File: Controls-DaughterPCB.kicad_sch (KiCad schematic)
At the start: 17 parts, among them U8 LMC555xM

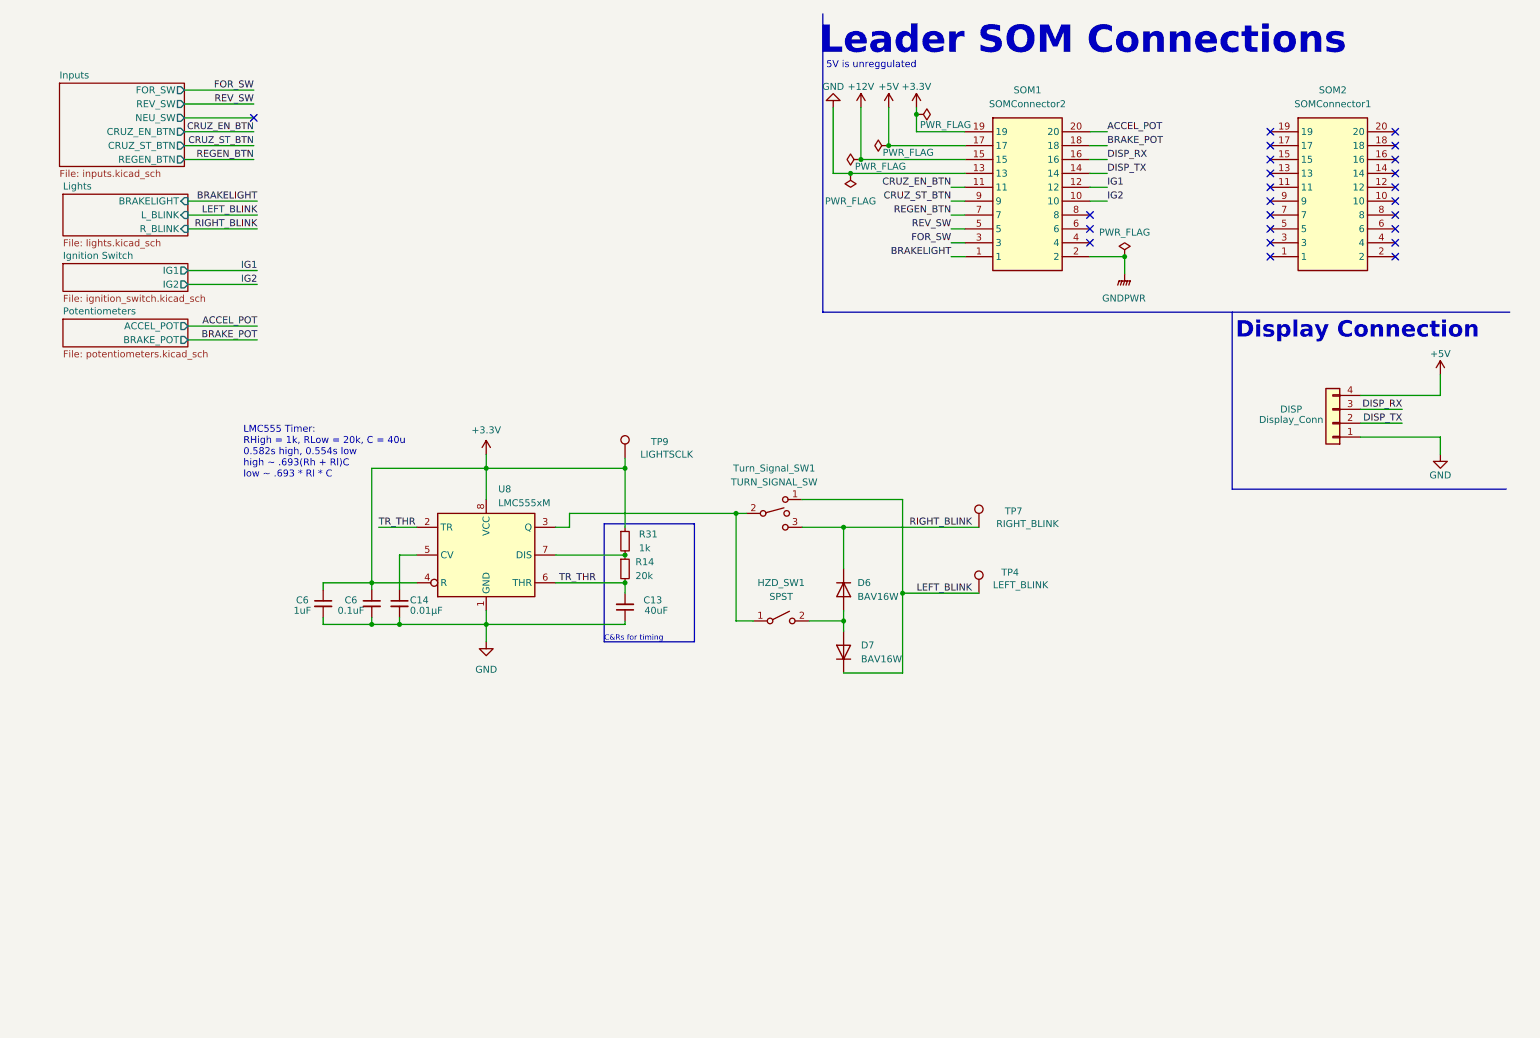
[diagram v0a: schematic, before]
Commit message: changed resistor values, updated footprints
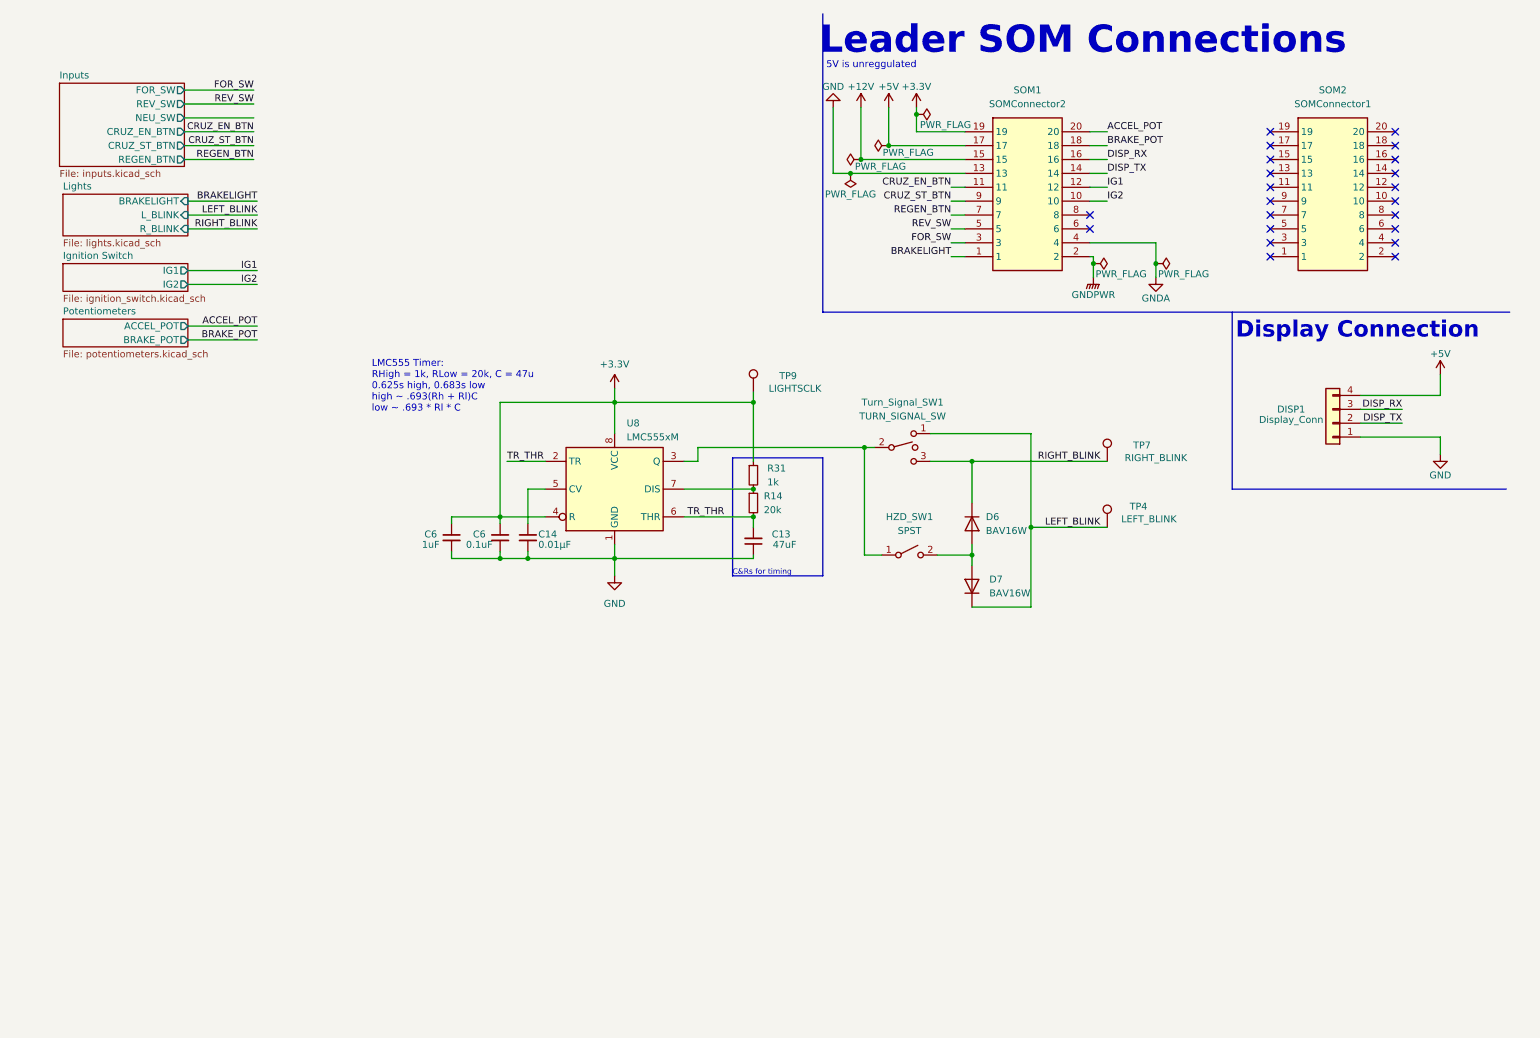
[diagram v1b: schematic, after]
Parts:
- C13: value 40uF -> 47uF; footprint (none) -> Capacitor_SMD:C_0805_2012Metric; Mouser Part Number (none) -> 81-GRM21BR61A476ME5L; P/N (none) -> GRM21BR61A476ME15L
- C14: footprint (none) -> Capacitor_SMD:C_0805_2012Metric; Mouser Part Number (none) -> 80-C0805C103J5R; P/N (none) -> C0805C103J5RACTU
- C6: footprint (none) -> Capacitor_SMD:C_0805_2012Metric; Mouser Part Number (none) -> 80-C0805C105K5P; P/N (none) -> C0805C105K5PACTU
- C6: footprint (none) -> Capacitor_SMD:C_0805_2012Metric; Mouser Part Number (none) -> 80-C0805C104M5R; P/N (none) -> C0805C104M5RACTU
- DISP1: renamed from DISP; footprint (none) -> Connector_Molex:Molex_Micro-Fit_3.0_43650-0415_1x04_P3.00mm_Vertical; Mouser Part Number (none) -> 538-43650-0415; P/N (none) -> 43650-0415
- R14: footprint (none) -> Resistor_SMD:R_0805_2012Metric; Mouser Part Number (none) -> 603-RP0805BRD0720KL; P/N (none) -> RP0805BRD0720KL
- R31: footprint (none) -> Resistor_SMD:R_0805_2012Metric; Mouser Part Number (none) -> 71-CRCW08051K00FKEAC; P/N (none) -> CRCW08051K00FKEAC
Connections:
- net GNDA: now reaches SOM1.4
- no-connect marks 24 -> 22
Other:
- note added: "LMC555 Timer: RHigh = 1k, RLow = 20k, C = 47u 0.625s high, 0.683s low high ~ .693(Rh + Rl)C low ~ .693 * Rl * C"
- note removed: "LMC555 Timer: RHigh = 1k, RLow = 20k, C = 40u 0.582s high, 0.554s low high ~ .693(Rh + Rl)C low ~ .693 * Rl * C"
- moved on the sheet: C13, C14, C6, D6, D7, HZD_SW1, R14, R31, TP4, TP7, TP9, Turn_Signal_SW1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

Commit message: added mounting holes & silkscreen images, created fans sheet
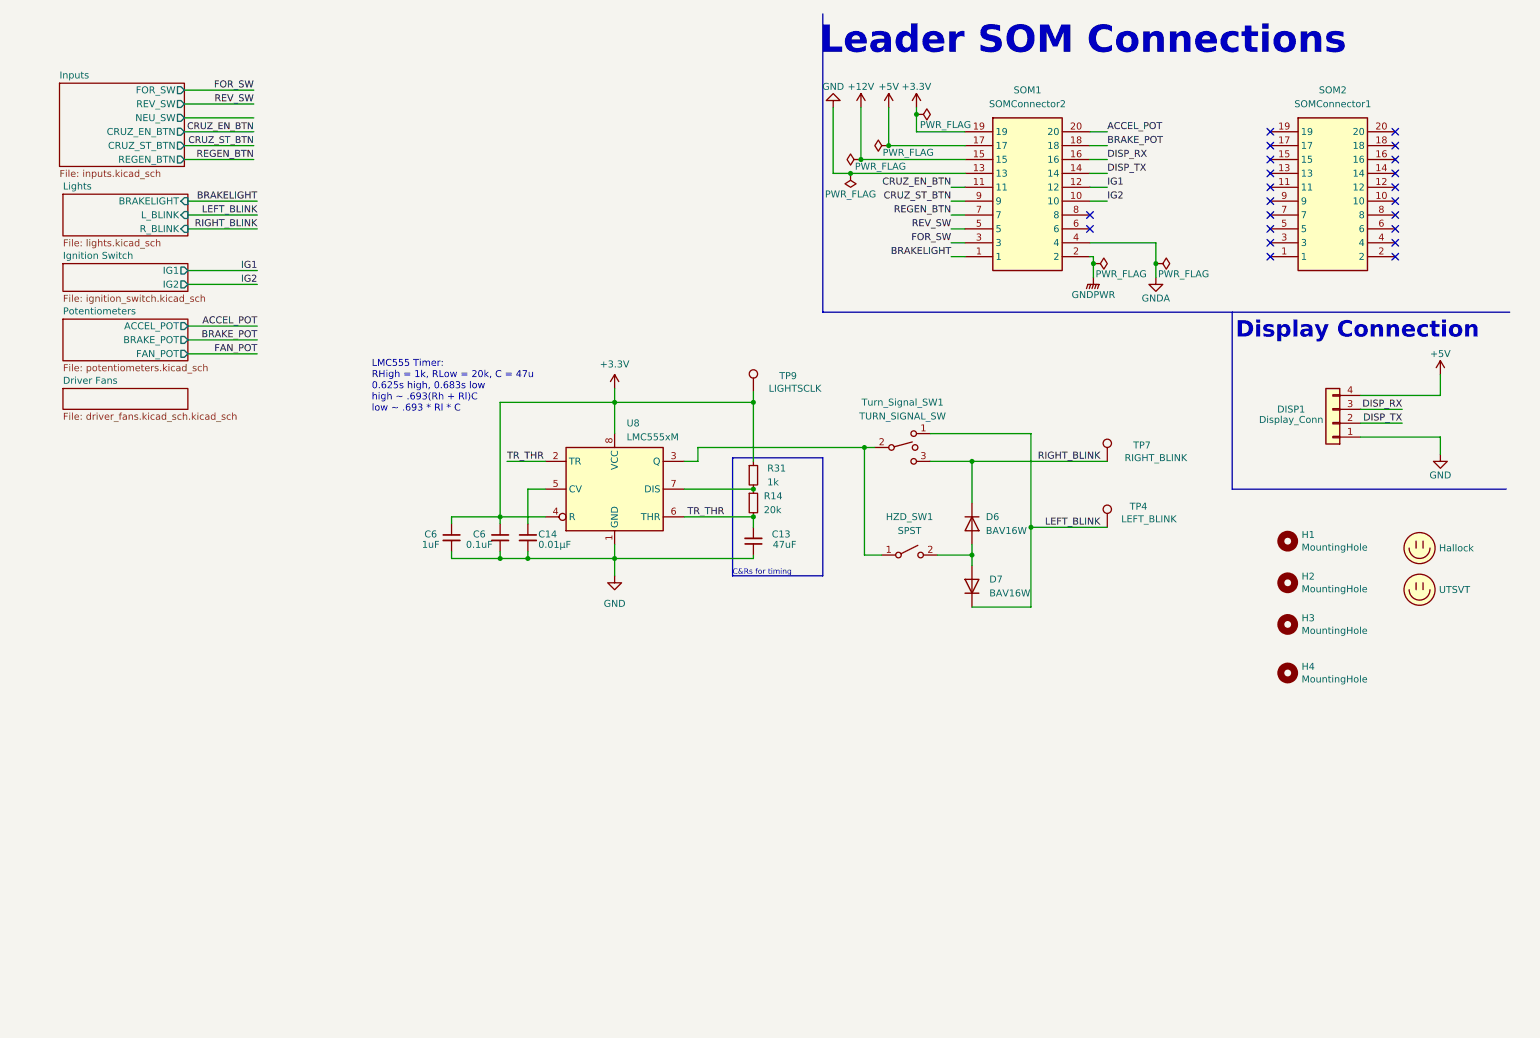
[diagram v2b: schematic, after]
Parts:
- added H1, H2, H3, H4: MountingHole, MountingHole:MountingHole_3mm, symbol Mechanical:MountingHole
- added LOGO1: Hallock, UTSVT_Special:Hallock_Image_Small, symbol utsvt-misc:Logo_Placeholder
- added LOGO2: UTSVT, UTSVT_Special:UTSVT_Logo_Symbol, symbol utsvt-misc:Logo_Placeholder
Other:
- added sheet Driver Fans (driver_fans.kicad_sch.kicad_sch)
- sheet Potentiometers ports: added FAN_POT; removed none
- note removed: "5V is unreggulated"
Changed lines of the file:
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@@
+    (stroke (width 0) (type default))
+  )
+  (wire (pts (xy 44.45 73.66) (xy 57.15 73.66))
     (stroke (width 0) (type default))
   )
@@
     (effects (font (size 1.27 1.27)) (justify left bottom))
   )
-  (text "5V is unreggulated\n" (at 161.29 21.59 0)
-    (effects (font (size 1.27 1.27)) (justify left bottom))
-  )
   (label "REGEN_BTN" (at 56.515 38.1 180) (fields_autoplaced)
     (effects (font (size 1.27 1.27)) (justify right bottom))
@@
   (label "DISP_RX" (at 212.725 38.1 0) (fields_autoplaced)
     (effects (font (size 1.27 1.27)) (justify left bottom))
+  )
+  (label "FAN_POT" (at 57.15 73.66 180) (fields_autoplaced)
+    (effects (font (size 1.27 1.27)) (justify right bottom))
   )
   (label "ACCEL_POT" (at 212.725 33.02 0) (fields_autoplaced)
@@
     )
   )
+  (symbol (lib_id "Mechanical:MountingHole") (at 245.745 115.57 0) (unit 1)
+    (in_bom yes) (on_board yes) (dnp no)
+    (property "Reference" "H2" (at 248.285 114.4016 0)
+      (effects (font (size 1.27 1.27)) (justify left))
+    )
+    (property "Value" "MountingHole" (at 248.285 116.713 0)
+      (effects (font (size 1.27 1.27)) (justify left))
+    )
+    (property "Footprint" "MountingHole:MountingHole_3mm" (at 245.745 115.57 0)
+      (effects (font (size 1.27 1.27)) hide)
+    )
+    (property "Datasheet" "~" (at 245.745 115.57 0)
+      (effects (font (size 1.27 1.27)) hide)
+    )
+    (instances
+      (project "Controls-DaughterPCB"
+        (path "/c7871779-04fe-4705-8150-20a4dd0ef44f"
+          (reference "H2") (unit 1)
+        )
+      )
+      (project "BPS-Fan"
+        (path "/e60847d4-a954-40b9-b9c4-54b73957661c"
+          (reference "H2") (unit 1)
+        )
+      )
+    )
+  )
   (symbol (lib_id "Connector:TestPoint") (at 212.725 105.41 0) (unit 1)
     (in_bom yes) (on_board yes) (dnp no)
@@
         (path "/c7871779-04fe-4705-8150-20a4dd0ef44f"
           (reference "#FLG01") (unit 1)
+        )
+      )
+    )
+  )
+  (symbol (lib_id "utsvt-misc:Logo_Placeholder") (at 269.875 109.22 0) (unit 1)
+    (in_bom yes) (on_board yes) (dnp no)
+    (property "Reference" "LOGO1" (at 269.875 105.41 0)
+      (effects (font (size 1.27 1.27)) hide)
+    )
+    (property "Value" "Hallock" (at 273.431 109.22 0)
+      (effects (font (size 1.27 1.27)) (justify left))
+    )
+    (property "Footprint" "UTSVT_Special:Hallock_Image_Small" (at 269.875 107.315 0)
+      (effects (font (size 1.27 1.27)) hide)
+    )
+    (property "Datasheet" "" (at 269.875 107.315 0)
+      (effects (font (size 1.27 1.27)) hide)
+    )
+    (instances
+      (project "Controls-DaughterPCB"
+        (path "/c7871779-04fe-4705-8150-20a4dd0ef44f"
+          (reference "LOGO1") (unit 1)
+        )
+      )
+      (project "BPS-Fan"
+        (path "/e60847d4-a954-40b9-b9c4-54b73957661c"
+          (reference "LOGO1") (unit 1)
         )
       )
@@
     )
   )
+  (symbol (lib_id "Mechanical:MountingHole") (at 245.745 132.08 0) (unit 1)
+    (in_bom yes) (on_board yes) (dnp no)
+    (property "Reference" "H4" (at 248.285 130.9116 0)
+      (effects (font (size 1.27 1.27)) (justify left))
+    )
+    (property "Value" "MountingHole" (at 248.285 133.223 0)
+      (effects (font (size 1.27 1.27)) (justify left))
+    )
+    (property "Footprint" "MountingHole:MountingHole_3mm" (at 245.745 132.08 0)
+      (effects (font (size 1.27 1.27)) hide)
+    )
+    (property "Datasheet" "~" (at 245.745 132.08 0)
+      (effects (font (size 1.27 1.27)) hide)
+    )
+    (instances
+      (project "Controls-DaughterPCB"
+        (path "/c7871779-04fe-4705-8150-20a4dd0ef44f"
+          (reference "H4") (unit 1)
+        )
+      )
+      (project "BPS-Fan"
+        (path "/e60847d4-a954-40b9-b9c4-54b73957661c"
+          (reference "H4") (unit 1)
+        )
+      )
+    )
+  )
   (symbol (lib_id "Device:C_Small") (at 106.68 107.315 0) (unit 1)
     (in_bom yes) (on_board yes) (dnp no)
@@
     )
   )
+  (symbol (lib_id "utsvt-misc:Logo_Placeholder") (at 269.875 116.84 0) (unit 1)
+    (in_bom yes) (on_board yes) (dnp no)
+    (property "Reference" "LOGO2" (at 269.875 113.03 0)
+      (effects (font (size 1.27 1.27)) hide)
+    )
+    (property "Value" "UTSVT" (at 273.431 116.84 0)
+      (effects (font (size 1.27 1.27)) (justify left))
+    )
+    (property "Footprint" "UTSVT_Special:UTSVT_Logo_Symbol" (at 269.875 114.935 0)
+      (effects (font (size 1.27 1.27)) hide)
+    )
+    (property "Datasheet" "" (at 269.875 114.935 0)
+      (effects (font (size 1.27 1.27)) hide)
+    )
+    (instances
+      (project "Controls-DaughterPCB"
+        (path "/c7871779-04fe-4705-8150-20a4dd0ef44f"
+          (reference "LOGO2") (unit 1)
+        )
+      )
+      (project "BPS-Fan"
+        (path "/e60847d4-a954-40b9-b9c4-54b73957661c"
+          (reference "LOGO2") (unit 1)
+        )
+      )
+    )
+  )
   (symbol (lib_id "power:PWR_FLAG") (at 177.8 29.845 270) (unit 1)
     (in_bom yes) (on_board yes) (dnp no)
@@
         (path "/c7871779-04fe-4705-8150-20a4dd0ef44f"
           (reference "#FLG02") (unit 1)
+        )
+      )
+    )
+  )
+  (symbol (lib_id "Mechanical:MountingHole") (at 245.745 107.95 0) (unit 1)
+    (in_bom yes) (on_board yes) (dnp no)
+    (property "Reference" "H1" (at 248.285 106.7816 0)
+      (effects (font (size 1.27 1.27)) (justify left))
+    )
+    (property "Value" "MountingHole" (at 248.285 109.093 0)
+      (effects (font (size 1.27 1.27)) (justify left))
+    )
+    (property "Footprint" "MountingHole:MountingHole_3mm" (at 245.745 107.95 0)
+      (effects (font (size 1.27 1.27)) hide)
+    )
+    (property "Datasheet" "~" (at 245.745 107.95 0)
+      (effects (font (size 1.27 1.27)) hide)
+    )
+    (instances
+      (project "Controls-DaughterPCB"
+        (path "/c7871779-04fe-4705-8150-20a4dd0ef44f"
+          (reference "H1") (unit 1)
+        )
+      )
+      (project "BPS-Fan"
+        (path "/e60847d4-a954-40b9-b9c4-54b73957661c"
+          (reference "H1") (unit 1)
         )
       )
@@
     )
   )
+  (symbol (lib_id "Mechanical:MountingHole") (at 245.745 123.19 0) (unit 1)
+    (in_bom yes) (on_board yes) (dnp no)
+    (property "Reference" "H3" (at 248.285 122.0216 0)
+      (effects (font (size 1.27 1.27)) (justify left))
+    )
+    (property "Value" "MountingHole" (at 248.285 124.333 0)
+      (effects (font (size 1.27 1.27)) (justify left))
+    )
+    (property "Footprint" "MountingHole:MountingHole_3mm" (at 245.745 123.19 0)
+      (effects (font (size 1.27 1.27)) hide)
+    )
+    (property "Datasheet" "~" (at 245.745 123.19 0)
+      (effects (font (size 1.27 1.27)) hide)
+    )
+    (instances
+      (project "Controls-DaughterPCB"
+        (path "/c7871779-04fe-4705-8150-20a4dd0ef44f"
+          (reference "H3") (unit 1)
+        )
+      )
+      (project "BPS-Fan"
+        (path "/e60847d4-a954-40b9-b9c4-54b73957661c"
+          (reference "H3") (unit 1)
+        )
+      )
+    )
+  )
   (symbol (lib_id "Device:R_Small") (at 147.955 95.885 0) (unit 1)
     (in_bom yes) (on_board yes) (dnp no) (fields_autoplaced)
@@
     )
   )
-  (sheet (at 21.59 67.31) (size 22.86 5.08) (fields_autoplaced)
+  (sheet (at 21.59 67.31) (size 22.86 7.62) (fields_autoplaced)
     (stroke (width 0.1524) (type solid))
     (fill (color 0 0 0 0.0000))
@@
       (effects (font (size 1.27 1.27)) (justify left bottom))
     )
-    (property "Sheetfile" "potentiometers.kicad_sch" (at 21.59 72.9746 0)
+    (property "Sheetfile" "potentiometers.kicad_sch" (at 21.59 75.5146 0)
       (effects (font (size 1.27 1.27)) (justify left top))
     )
@@
     )
     (pin "BRAKE_POT" output (at 44.45 71.12 0)
+      (effects (font (size 1.27 1.27)) (justify right))
+    )
+    (pin "FAN_POT" output (at 44.45 73.66 0)
       (effects (font (size 1.27 1.27)) (justify right))
     )
@@
       )
     )
+  )
+  (sheet (at 21.59 80.01) (size 22.86 3.81) (fields_autoplaced)
+    (stroke (width 0.1524) (type solid))
+    (fill (color 0 0 0 0.0000))
+    (property "Sheetname" "Driver Fans" (at 21.59 79.2984 0)
+      (effects (font (size 1.27 1.27)) (justify left bottom))
+    )
+    (property "Sheetfile" "driver_fans.kicad_sch.kicad_sch" (at 21.59 84.4046 0)
+      (effects (font (size 1.27 1.27)) (justify left top))
+    )
+    (instances
+      (project "Controls-DaughterPCB"
+        (path "/c7871779-04fe-4705-8150-20a4dd0ef44f" (page "6"))
+      )
+    )
